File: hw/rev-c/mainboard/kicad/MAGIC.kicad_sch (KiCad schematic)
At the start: 16 parts, among them U7 SN74LVC4245APWR, U8 SN74LVC4245APWR, U9 SN74LVC4245APWR

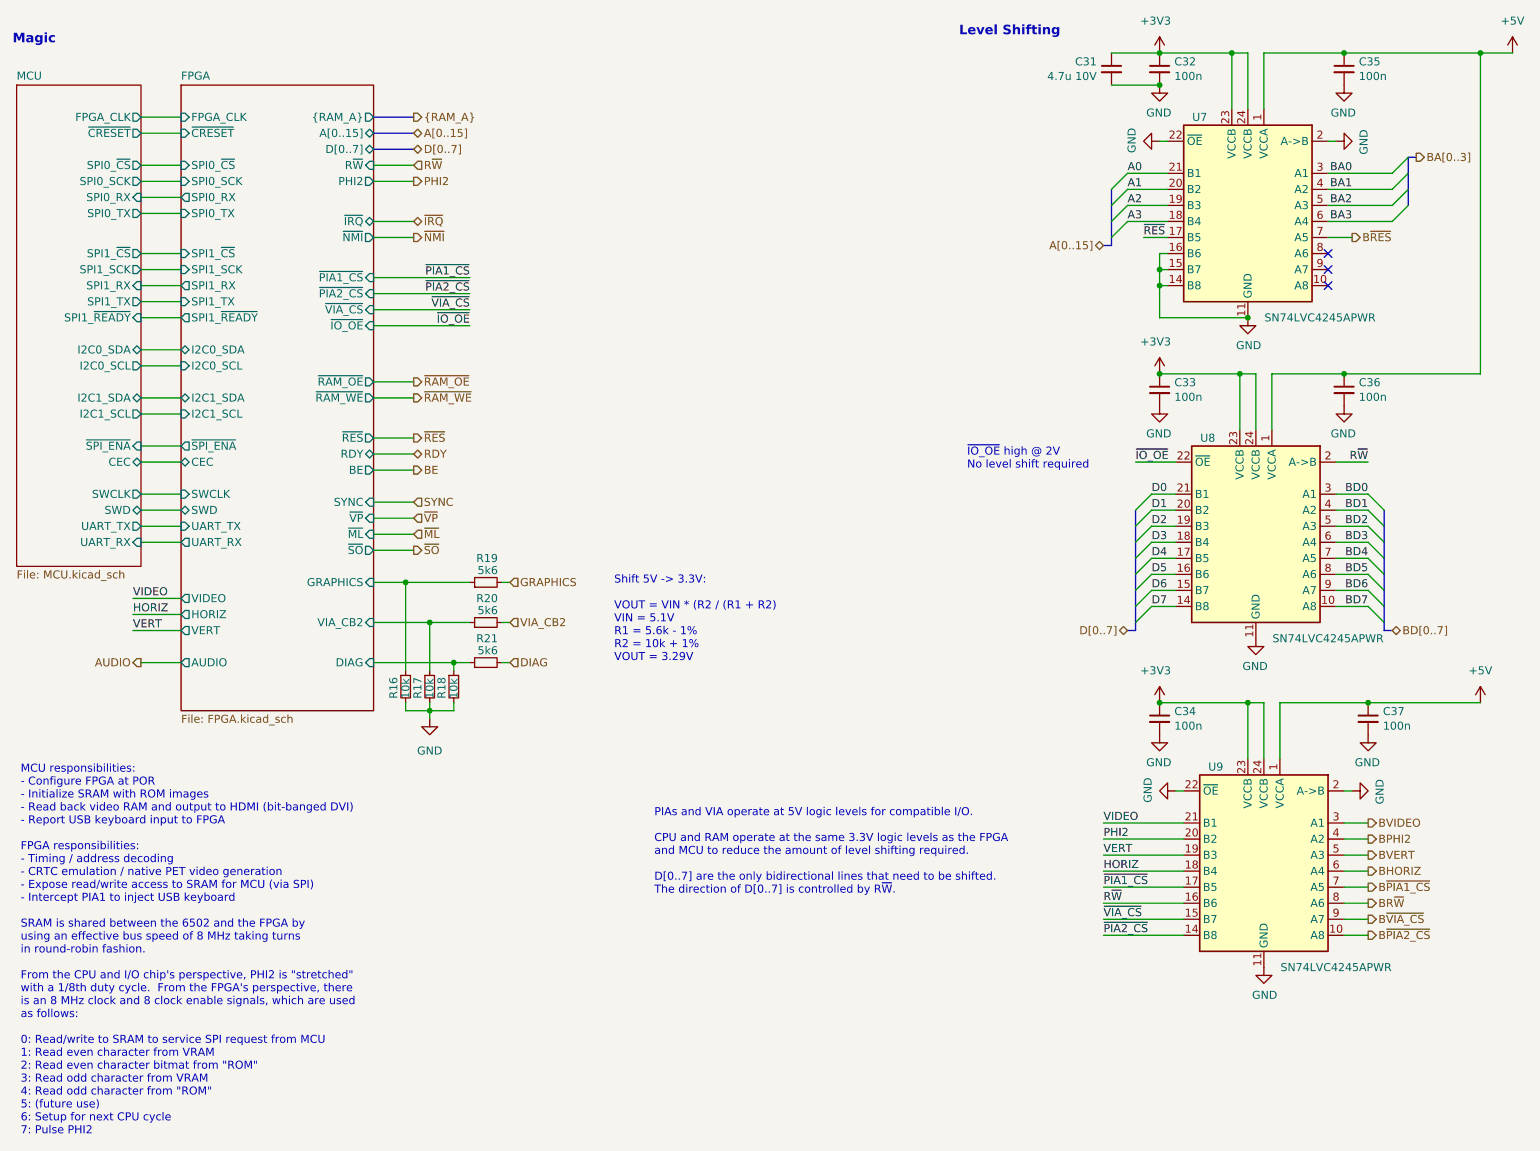
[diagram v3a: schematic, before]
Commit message: hw: match original PET designators for connectors
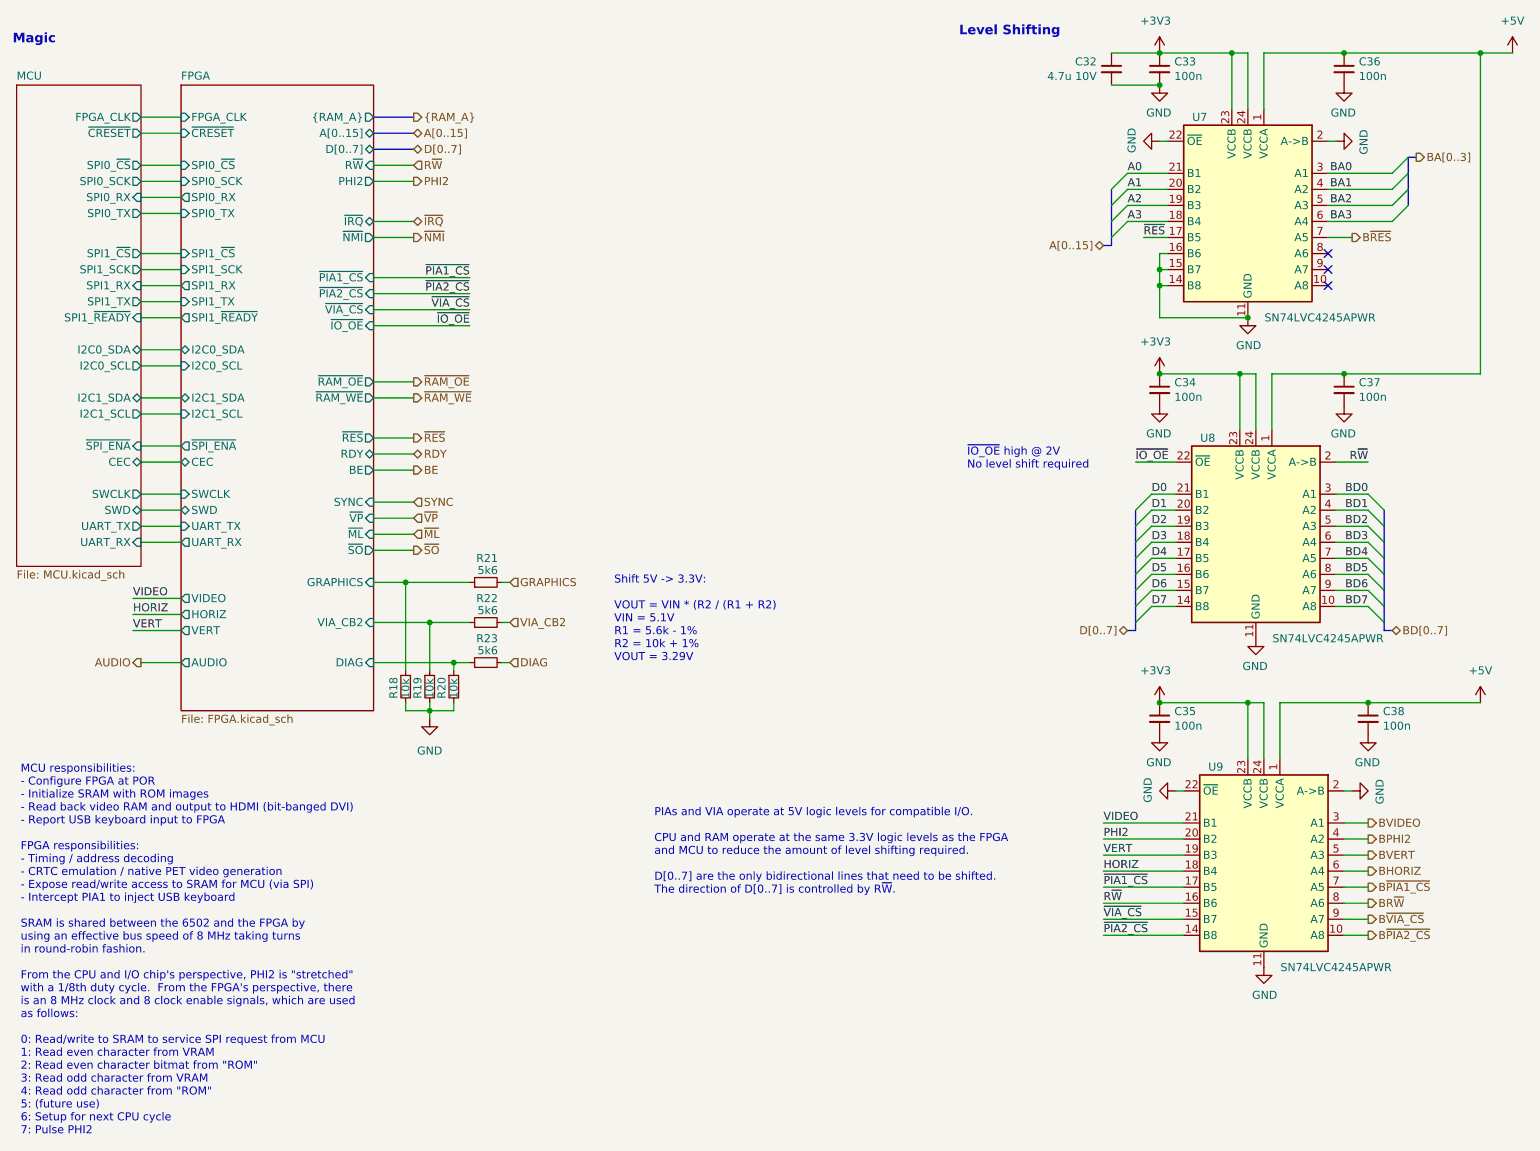
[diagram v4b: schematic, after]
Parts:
- renumbered C31 to C32, C32 to C33, C33 to C34, C34 to C35, C35 to C36, C36 to C37, C37 to C38, R16 to R18, R17 to R19, R18 to R20, R19 to R21, R20 to R22, R21 to R23
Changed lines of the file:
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@@
 		(on_board yes)
 		(dnp no)
-		(property "Reference" "C32"
+		(property "Reference" "C33"
 			(at 209.3468 21.6916 0)
 			(effects
@@
 			(project ""
 				(path "/2eea20e6-112c-411a-b615-885ae773135a/00000000-0000-0000-0000-0000617d6918"
-					(reference "C32")
+					(reference "C33")
 					(unit 1)
 				)
@@
 		(on_board yes)
 		(dnp no)
-		(property "Reference" "C34"
+		(property "Reference" "C35"
 			(at 209.3468 124.5616 0)
 			(effects
@@
 			(project ""
 				(path "/2eea20e6-112c-411a-b615-885ae773135a/00000000-0000-0000-0000-0000617d6918"
-					(reference "C34")
+					(reference "C35")
 					(unit 1)
 				)
@@
 		(on_board yes)
 		(dnp no)
-		(property "Reference" "C35"
+		(property "Reference" "C36"
 			(at 238.5568 21.6916 0)
 			(effects
@@
 			(project ""
 				(path "/2eea20e6-112c-411a-b615-885ae773135a/00000000-0000-0000-0000-0000617d6918"
-					(reference "C35")
+					(reference "C36")
 					(unit 1)
 				)
@@
 		(on_board yes)
 		(dnp no)
-		(property "Reference" "C37"
+		(property "Reference" "C38"
 			(at 242.3668 124.5616 0)
 			(effects
@@
 			(project ""
 				(path "/2eea20e6-112c-411a-b615-885ae773135a/00000000-0000-0000-0000-0000617d6918"
-					(reference "C37")
+					(reference "C38")
 					(unit 1)
 				)
@@
 		(on_board yes)
 		(dnp no)
-		(property "Reference" "C36"
+		(property "Reference" "C37"
 			(at 238.5568 72.4916 0)
 			(effects
@@
 			(project ""
 				(path "/2eea20e6-112c-411a-b615-885ae773135a/00000000-0000-0000-0000-0000617d6918"
-					(reference "C36")
+					(reference "C37")
 					(unit 1)
 				)
@@
 		(on_board yes)
 		(dnp no)
-		(property "Reference" "C33"
+		(property "Reference" "C34"
 			(at 209.3468 72.4916 0)
 			(effects
@@
 			(project ""
 				(path "/2eea20e6-112c-411a-b615-885ae773135a/00000000-0000-0000-0000-0000617d6918"
-					(reference "C33")
+					(reference "C34")
 					(unit 1)
 				)
@@
 		(on_board yes)
 		(dnp no)
-		(property "Reference" "R21"
+		(property "Reference" "R23"
 			(at 102.235 113.03 90)
 			(effects
@@
 			(project ""
 				(path "/2eea20e6-112c-411a-b615-885ae773135a/00000000-0000-0000-0000-0000617d6918"
-					(reference "R21")
+					(reference "R23")
 					(unit 1)
 				)
@@
 		(on_board yes)
 		(dnp no)
-		(property "Reference" "R20"
+		(property "Reference" "R22"
 			(at 102.235 106.68 90)
 			(effects
@@
 			(project ""
 				(path "/2eea20e6-112c-411a-b615-885ae773135a/00000000-0000-0000-0000-0000617d6918"
-					(reference "R20")
+					(reference "R22")
 					(unit 1)
 				)
@@
 		(on_board yes)
 		(dnp no)
-		(property "Reference" "R19"
+		(property "Reference" "R21"
 			(at 102.235 100.33 90)
 			(effects
@@
 			(project ""
 				(path "/2eea20e6-112c-411a-b615-885ae773135a/00000000-0000-0000-0000-0000617d6918"
-					(reference "R19")
+					(reference "R21")
 					(unit 1)
 				)
@@
 		(on_board yes)
 		(dnp no)
-		(property "Reference" "R18"
+		(property "Reference" "R20"
 			(at 93.345 122.555 90)
 			(effects
@@
 			(project ""
 				(path "/2eea20e6-112c-411a-b615-885ae773135a/00000000-0000-0000-0000-0000617d6918"
-					(reference "R18")
+					(reference "R20")
 					(unit 1)
 				)
@@
 		(on_board yes)
 		(dnp no)
-		(property "Reference" "C31"
+		(property "Reference" "C32"
 			(at 197.0532 21.6916 0)
 			(effects
@@
 			(project ""
 				(path "/2eea20e6-112c-411a-b615-885ae773135a/00000000-0000-0000-0000-0000617d6918"
-					(reference "C31")
+					(reference "C32")
 					(unit 1)
 				)
@@
 		(on_board yes)
 		(dnp no)
-		(property "Reference" "R16"
+		(property "Reference" "R18"
 			(at 85.725 122.555 90)
 			(effects
@@
 			(project ""
 				(path "/2eea20e6-112c-411a-b615-885ae773135a/00000000-0000-0000-0000-0000617d6918"
-					(reference "R16")
+					(reference "R18")
 					(unit 1)
 				)
@@
 		(on_board yes)
 		(dnp no)
-		(property "Reference" "R17"
+		(property "Reference" "R19"
 			(at 89.535 122.555 90)
 			(effects
@@
 			(project ""
 				(path "/2eea20e6-112c-411a-b615-885ae773135a/00000000-0000-0000-0000-0000617d6918"
-					(reference "R17")
-					(unit 1)
-				)
+					(reference "R19")
+					(unit 1)
+				)

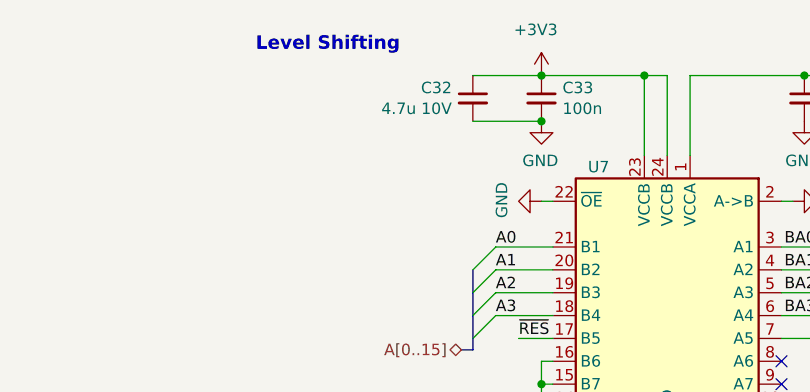
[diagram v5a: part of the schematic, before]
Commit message: hw: routing touchups, killer poke mitigation
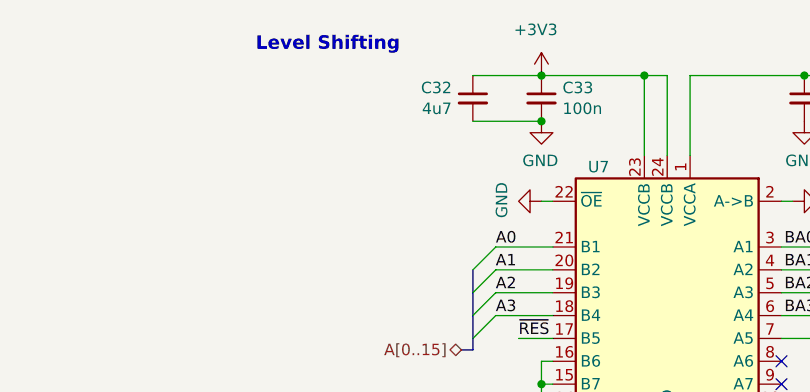
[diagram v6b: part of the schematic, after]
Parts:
- C32: value 4.7u 10V -> 4u7; LCSC C23733 -> C1538
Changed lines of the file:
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@@
 			)
 		)
-		(property "Value" "4.7u 10V"
+		(property "Value" "4u7"
 			(at 197.0532 24.003 0)
 			(effects
@@
 			)
 		)
-		(property "Datasheet" "https://product.samsungsem.com/mlcc/CL05A475MP5NRN.do"
+		(property "Datasheet" "https://www.lcsc.com/datasheet/lcsc_datasheet_2304140030_FH--Guangdong-Fenghua-Advanced-Tech-0402B472K500NT_C1538.pdf"
 			(at 199.39 22.86 0)
 			(effects
@@
 			)
 		)
-		(property "LCSC" "C23733"
+		(property "LCSC" "C1538"
 			(at 199.39 22.86 0)
 			(effects

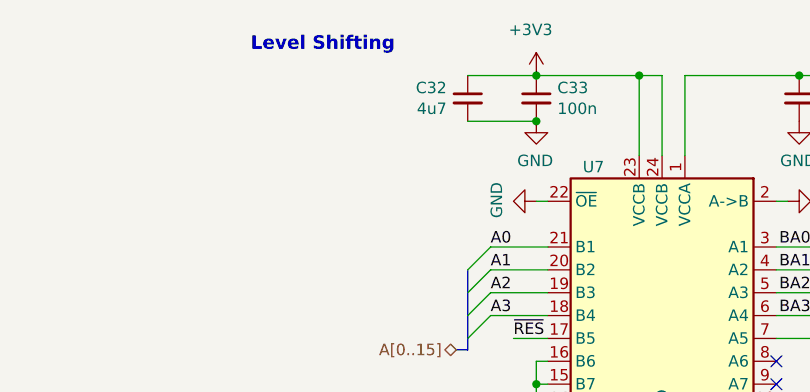
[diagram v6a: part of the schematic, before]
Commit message: hw: fix/update parts / use parallel resistors to control 5V
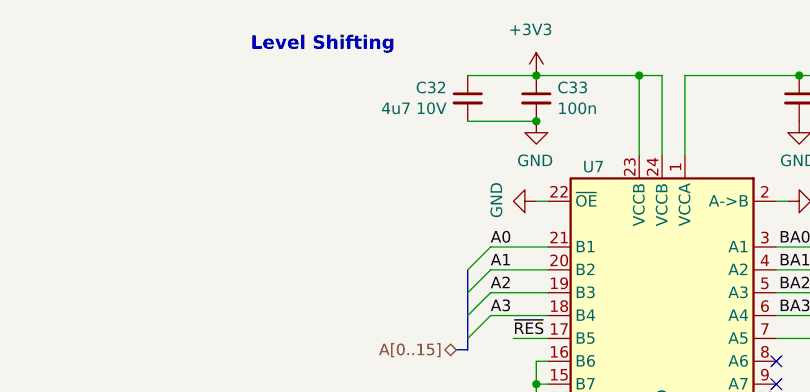
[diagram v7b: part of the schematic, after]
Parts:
- C32: value 4u7 -> 4u7 10V; LCSC C1538 -> C23733
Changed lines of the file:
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@@
 			)
 		)
-		(property "Datasheet" "https://datasheet.lcsc.com/lcsc/1809192324_Texas-Instruments-SN74LVC4245APWR_C7859.pdf"
+		(property "Datasheet" "https://www.lcsc.com/datasheet/lcsc_datasheet_1809192324_Texas-Instruments-SN74LVC4245APWR_C7859.pdf"
 			(at 222.25 50.8 0)
 			(effects
@@
 			)
 		)
-		(property "Datasheet" "https://datasheet.lcsc.com/lcsc/1809192324_Texas-Instruments-SN74LVC4245APWR_C7859.pdf"
+		(property "Datasheet" "https://www.lcsc.com/datasheet/lcsc_datasheet_1809192324_Texas-Instruments-SN74LVC4245APWR_C7859.pdf"
 			(at 224.79 153.67 0)
 			(effects
@@
 			)
 		)
-		(property "Datasheet" "https://datasheet.lcsc.com/lcsc/1809192324_Texas-Instruments-SN74LVC4245APWR_C7859.pdf"
+		(property "Datasheet" "https://www.lcsc.com/datasheet/lcsc_datasheet_1809192324_Texas-Instruments-SN74LVC4245APWR_C7859.pdf"
 			(at 223.52 101.6 0)
 			(effects
@@
 			)
 		)
-		(property "Datasheet" "https://datasheet.lcsc.com/lcsc/2304140030_Samsung-Electro-Mechanics-CL05B104KB54PNC_C307331.pdf"
+		(property "Datasheet" "https://product.samsungsem.com/mlcc/CL05B104KB54PN.do"
 			(at 207.01 22.86 0)
 			(effects
@@
 			)
 		)
-		(property "Datasheet" "https://datasheet.lcsc.com/lcsc/2304140030_Samsung-Electro-Mechanics-CL05B104KB54PNC_C307331.pdf"
+		(property "Datasheet" "https://product.samsungsem.com/mlcc/CL05B104KB54PN.do"
 			(at 207.01 125.73 0)
 			(effects
@@
 			)
 		)
-		(property "Datasheet" "https://datasheet.lcsc.com/lcsc/2304140030_Samsung-Electro-Mechanics-CL05B104KB54PNC_C307331.pdf"
+		(property "Datasheet" "https://product.samsungsem.com/mlcc/CL05B104KB54PN.do"
 			(at 236.22 22.86 0)
 			(effects
@@
 			)
 		)
-		(property "Datasheet" "https://datasheet.lcsc.com/lcsc/2304140030_Samsung-Electro-Mechanics-CL05B104KB54PNC_C307331.pdf"
+		(property "Datasheet" "https://product.samsungsem.com/mlcc/CL05B104KB54PN.do"
 			(at 240.03 125.73 0)
 			(effects
@@
 			)
 		)
-		(property "Datasheet" "https://datasheet.lcsc.com/lcsc/2304140030_Samsung-Electro-Mechanics-CL05B104KB54PNC_C307331.pdf"
+		(property "Datasheet" "https://product.samsungsem.com/mlcc/CL05B104KB54PN.do"
 			(at 236.22 73.66 0)
 			(effects
@@
 			)
 		)
-		(property "Datasheet" "https://datasheet.lcsc.com/lcsc/2304140030_Samsung-Electro-Mechanics-CL05B104KB54PNC_C307331.pdf"
+		(property "Datasheet" "https://product.samsungsem.com/mlcc/CL05B104KB54PN.do"
 			(at 207.01 73.66 0)
 			(effects
@@
 			)
 		)
-		(property "Datasheet" "https://datasheet.lcsc.com/lcsc/2206010045_UNI-ROYAL-Uniroyal-Elec-0402WGF5601TCE_C25908.pdf"
+		(property "Datasheet" "https://www.lcsc.com/datasheet/lcsc_datasheet_2206010045_UNI-ROYAL-Uniroyal-Elec-0402WGF5601TCE_C25908.pdf"
 			(at 100.33 116.84 0)
 			(effects
@@
 			)
 		)
-		(property "Datasheet" "https://datasheet.lcsc.com/lcsc/2206010045_UNI-ROYAL-Uniroyal-Elec-0402WGF5601TCE_C25908.pdf"
+		(property "Datasheet" "https://www.lcsc.com/datasheet/lcsc_datasheet_2206010045_UNI-ROYAL-Uniroyal-Elec-0402WGF5601TCE_C25908.pdf"
 			(at 100.33 110.49 0)
 			(effects
@@
 			)
 		)
-		(property "Datasheet" "https://datasheet.lcsc.com/lcsc/2206010045_UNI-ROYAL-Uniroyal-Elec-0402WGF5601TCE_C25908.pdf"
+		(property "Datasheet" "https://www.lcsc.com/datasheet/lcsc_datasheet_2206010045_UNI-ROYAL-Uniroyal-Elec-0402WGF5601TCE_C25908.pdf"
 			(at 100.33 104.14 0)
 			(effects
@@
 			)
 		)
-		(property "Datasheet" "https://datasheet.lcsc.com/lcsc/2206010100_UNI-ROYAL-Uniroyal-Elec-0402WGF1002TCE_C25744.pdf"
+		(property "Datasheet" "https://jlcpcb.com/api/file/downloadByFileSystemAccessId/8556212101498380288"
 			(at 95.25 120.65 0)
 			(effects
@@
 			)
 		)
-		(property "Value" "4u7"
+		(property "Value" "4u7 10V"
 			(at 197.0532 24.003 0)
 			(effects
@@
 			)
 		)
-		(property "Datasheet" "https://www.lcsc.com/datasheet/lcsc_datasheet_2304140030_FH--Guangdong-Fenghua-Advanced-Tech-0402B472K500NT_C1538.pdf"
+		(property "Datasheet" "https://product.samsungsem.com/mlcc/CL05A475MP5NRN.do"
 			(at 199.39 22.86 0)
 			(effects
@@
 			)
 		)
-		(property "LCSC" "C1538"
+		(property "LCSC" "C23733"
 			(at 199.39 22.86 0)
 			(effects
@@
 			)
 		)
-		(property "Datasheet" "https://datasheet.lcsc.com/lcsc/2206010100_UNI-ROYAL-Uniroyal-Elec-0402WGF1002TCE_C25744.pdf"
+		(property "Datasheet" "https://jlcpcb.com/api/file/downloadByFileSystemAccessId/8556212101498380288"
 			(at 87.63 120.65 0)
 			(effects
@@
 			)
 		)
-		(property "Datasheet" "https://datasheet.lcsc.com/lcsc/2206010100_UNI-ROYAL-Uniroyal-Elec-0402WGF1002TCE_C25744.pdf"
+		(property "Datasheet" "https://jlcpcb.com/api/file/downloadByFileSystemAccessId/8556212101498380288"
 			(at 91.44 120.65 0)
 			(effects
